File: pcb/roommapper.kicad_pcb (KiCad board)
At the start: 2 copper layers, 123.6 x 134.6 mm, 3 parts, among them U1 STM32F411CEUx_BlackPill, U2 RPLIDAR_C1

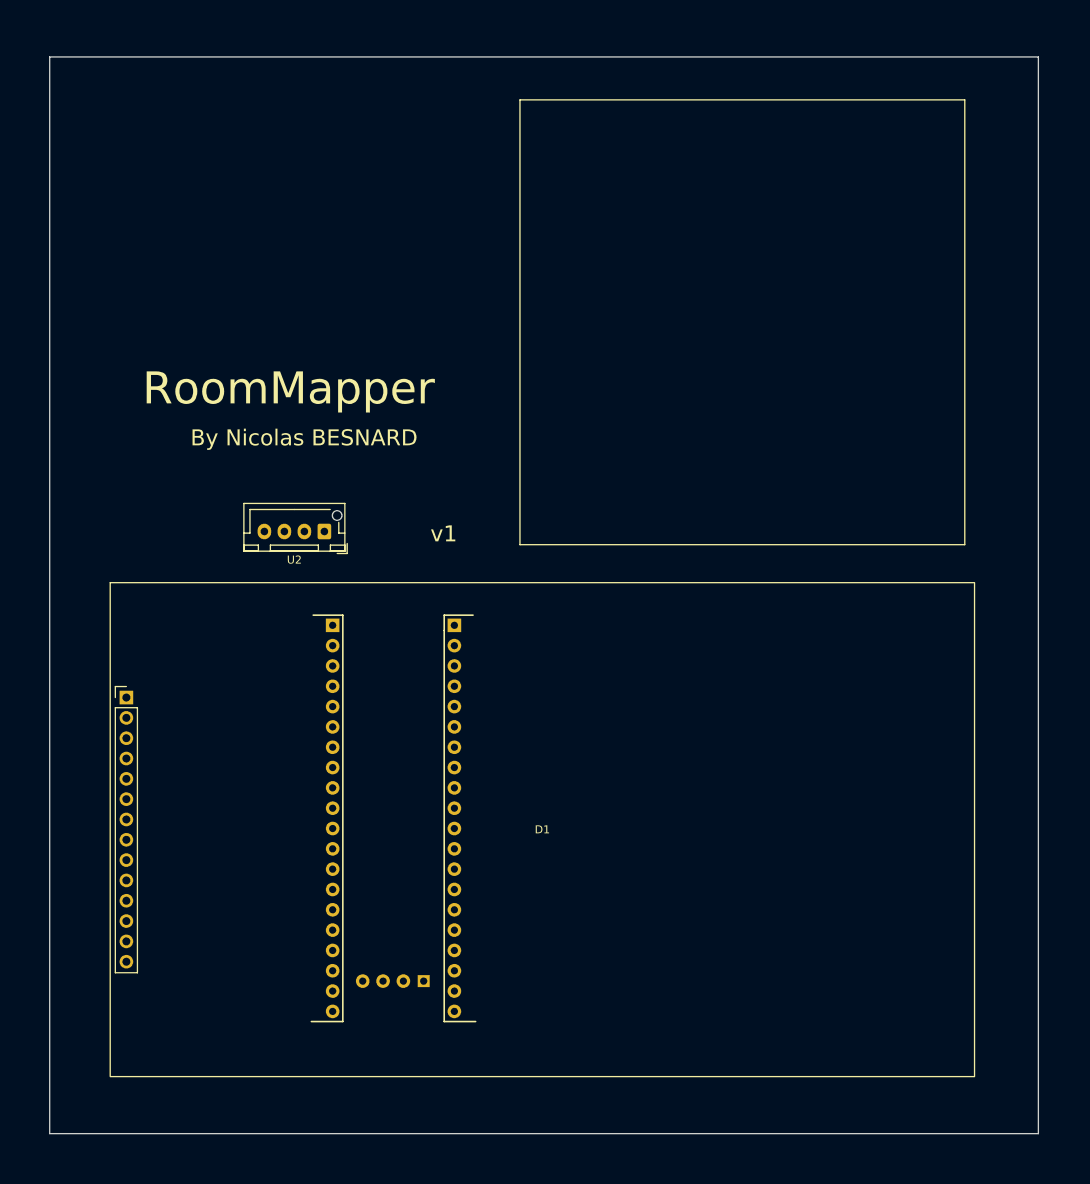
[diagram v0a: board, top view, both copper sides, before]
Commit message: general: update project io pins for easier pcb routing
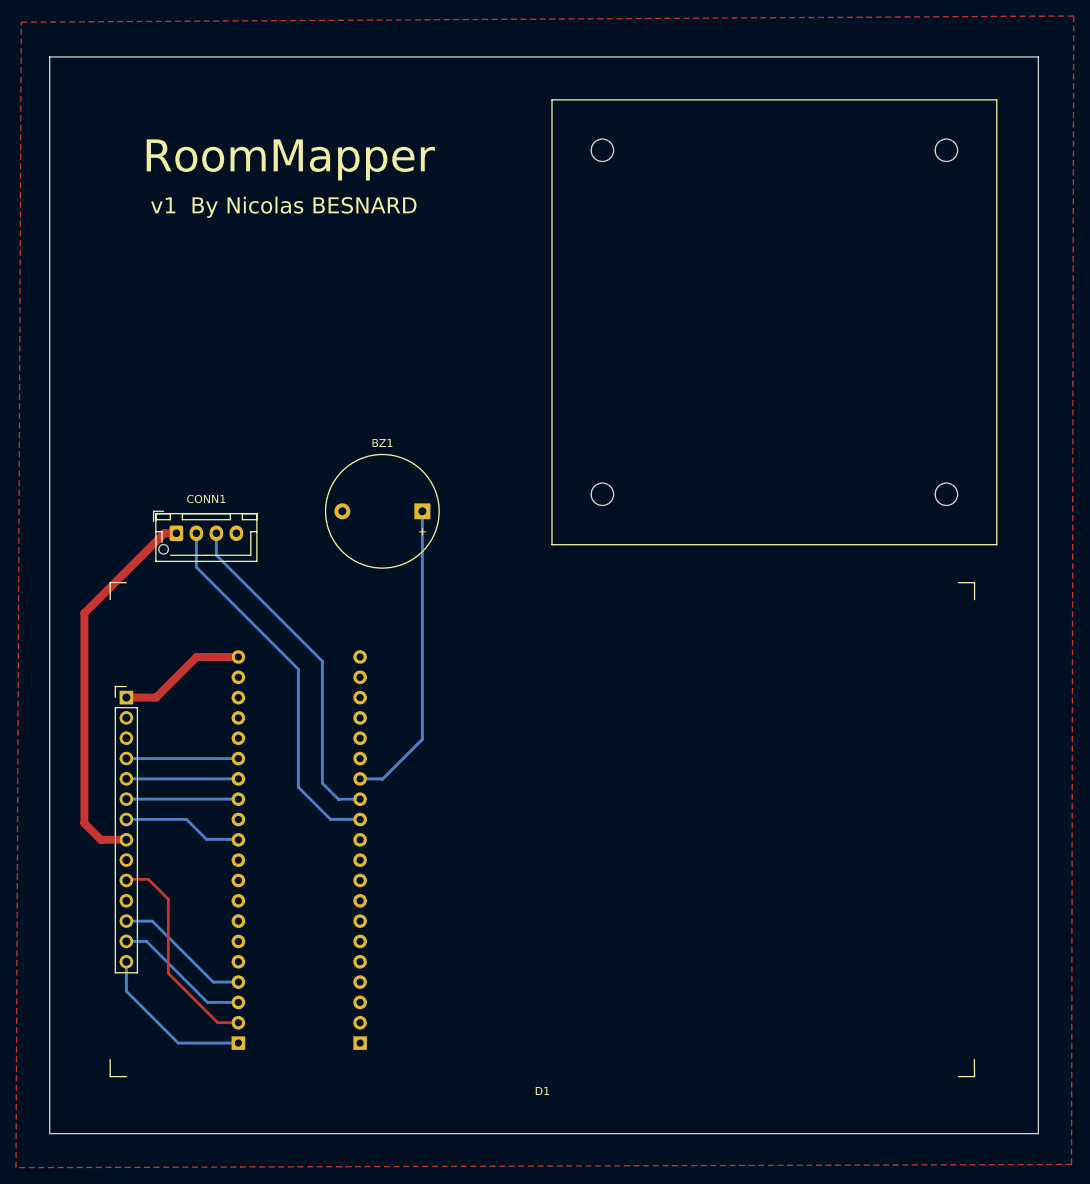
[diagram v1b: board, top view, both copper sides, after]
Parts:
- added BZ1: Buzzer, Buzzer_Beeper:Buzzer_D14mm_H7mm_P10mm, F.Cu at (108.0, 85.0)
- moved CONN1 18.5 mm to (77.2, 87.8), turned to 0 degrees
- moved U2 14.5 mm to (93.7, 125.6), turned to 90 degrees
- renumbered U2 to CONN1, U1 to U2
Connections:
- U2 pad 1: unconnected-(U1-PB12-Pad1) -> XPT2046_INT
- U2 pad 11: unconnected-(U1-PB3-Pad11) -> ILI94488_CLK
- U2 pad 13: unconnected-(U1-PB5-Pad13) -> ILI94488_MOSI
- U2 pad 14: unconnected-(U1-PB6-Pad14) -> ILI94488_DC
- U2 pad 15: unconnected-(U1-PB7-Pad15) -> ILI94488_RST
- U2 pad 27: unconnected-(U1-PA1-Pad27) -> BUZZER
- U2 pad 28: unconnected-(U1-PA2-Pad28) -> RPLIDAR_TX
- U2 pad 29: XPT2046_INT -> RPLIDAR_RX
- U2 pad 31: ILI94488_CLK -> unconnected-(U1-PA5-Pad31)
- U2 pad 33: ILI94488_MOSI -> unconnected-(U1-PA7-Pad33)
- U2 pad 36: ILI94488_RST -> unconnected-(U1-PB2-Pad36)
- U2 pad 37: ILI94488_DC -> unconnected-(U1-PB10-Pad37)
- U2 pad 6: RPLIDAR_TX -> unconnected-(U1-PA9-Pad6)
- U2 pad 7: RPLIDAR_RX -> unconnected-(U1-PA10-Pad7)
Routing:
- net 5V: track 0.00 -> 48.0 mm
- net RPLIDAR_RX: track 0.00 -> 46.4 mm
- net RPLIDAR_TX: track 0.00 -> 42.3 mm
- net BUZZER: track 0.00 -> 38.4 mm
- net XPT2046_CLK: track 0.00 -> 26.9 mm
- net XPT2046_INT: track 0.00 -> 20.4 mm
- net XPT2046_MISO: track 0.00 -> 17.2 mm
- net XPT2046_MOSI: track 0.00 -> 17.2 mm
- net 3.3V: track 0.00 -> 16.1 mm
- net ILI94488_CLK: track 0.00 -> 15.1 mm
- net ILI94488_RST: track 0.00 -> 14.0 mm
- net ILI94488_MOSI: track 0.00 -> 14.0 mm
- net ILI94488_DC: track 0.00 -> 14.0 mm
- added copper zone on F.Cu, net GND
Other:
- outline, holes or cut-outs redrawn

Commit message: pcb: update
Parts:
- BZ1: footprint Buzzer_Beeper:Buzzer_D14mm_H7mm_P10mm -> Buzzer_Beeper:Buzzer_12x9.5RM7.6
- CONN1: footprint Connector_JST:JST_XH_B4B-XH-AM_1x04_P2.50mm_Vertical -> Connector_JST:JST_XH_B4B-XH-A_1x04_P2.50mm_Vertical
- moved BZ1 6.00 mm to (108.0, 91.0)
- moved CONN1 2.00 mm to (77.2, 89.8)
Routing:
- net BUZZER: track 38.4 -> 32.4 mm
- net RPLIDAR_TX: track 42.3 -> 40.3 mm
- net RPLIDAR_RX: track 46.4 -> 44.4 mm
- net 5V: track 48.0 -> 47.2 mm
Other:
- board text removed: "v1"
